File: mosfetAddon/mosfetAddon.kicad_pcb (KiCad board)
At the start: 2 copper layers, 89 x 61 mm, 70 parts, among them J1 coil, J10 Conn_01x18_Male, J2 coil, J3 coil, J4 coil, J5 coil, J6 coil, J7 coil, J8 coil, J9 pow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

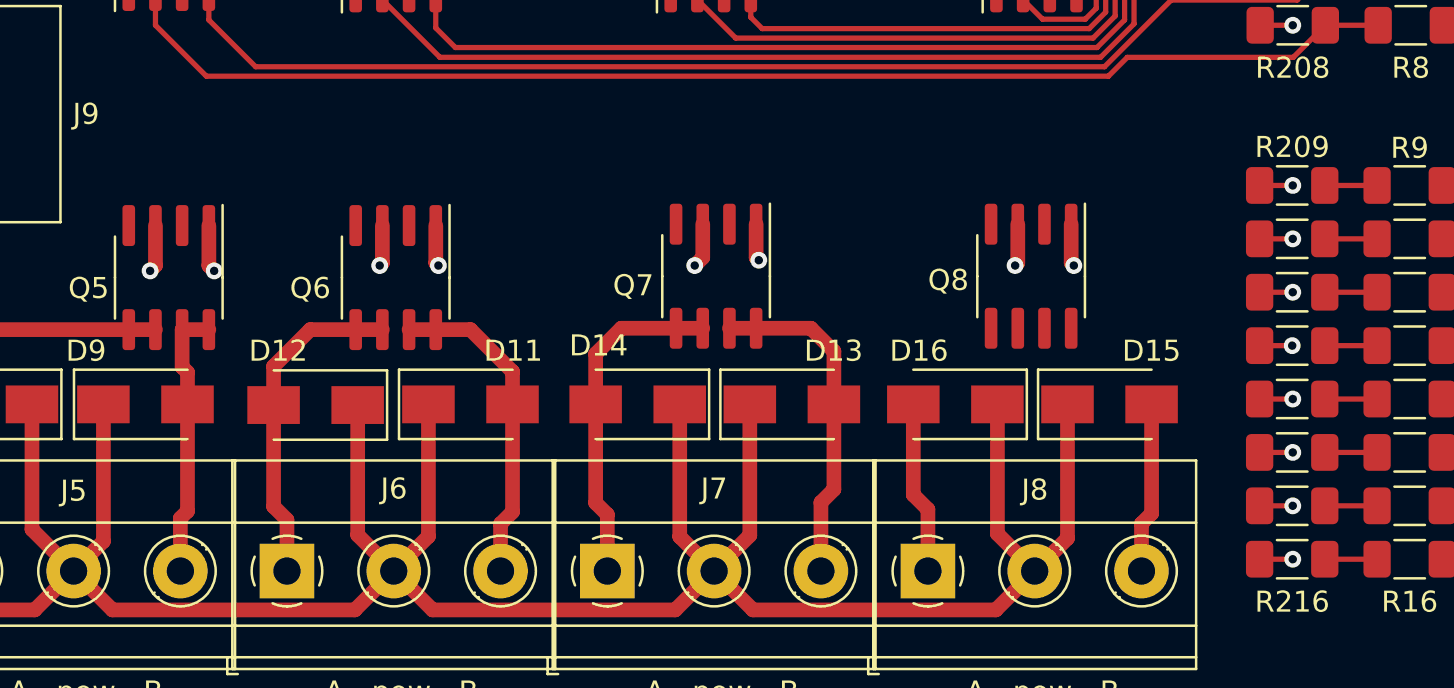
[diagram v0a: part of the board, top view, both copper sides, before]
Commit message: about to redo the PCB with an atmega 2560 instead. This will eliminate the need for 2 IO extenders and gives me the extra serial interface which I need. I also lack IO on the 328p
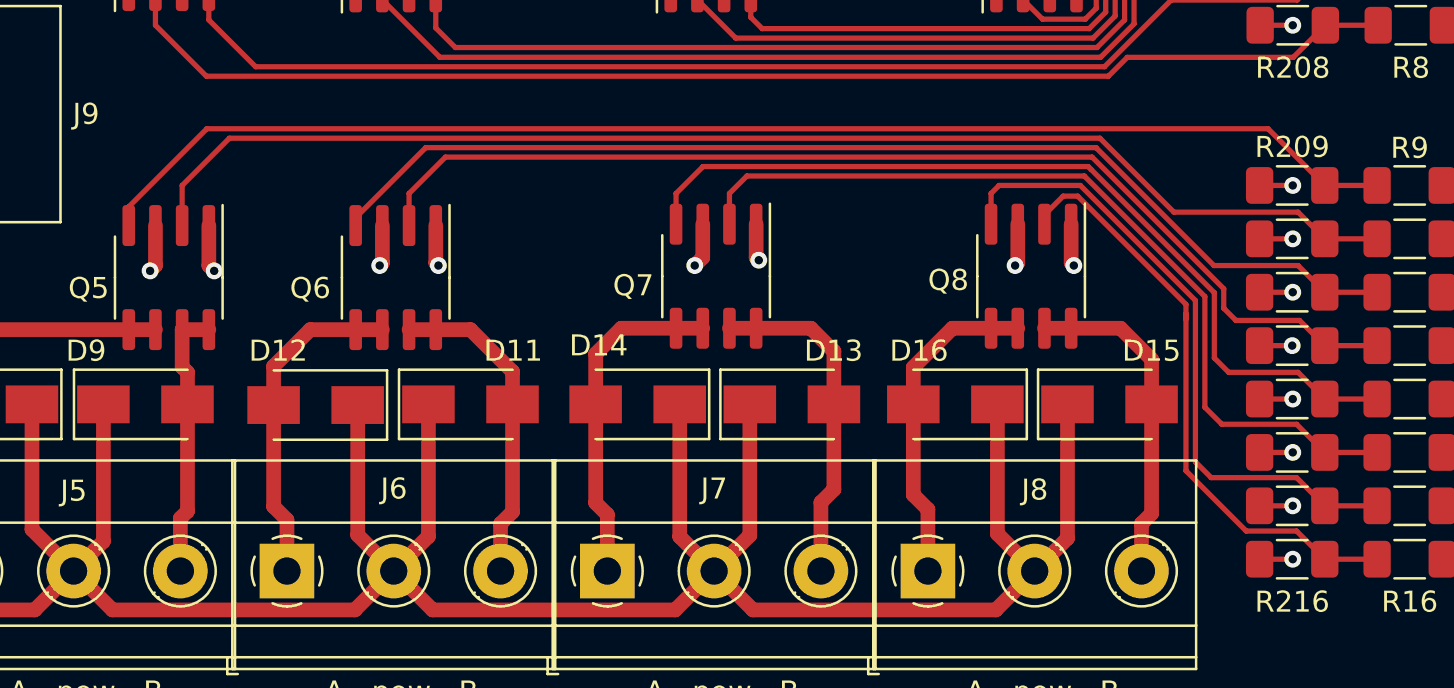
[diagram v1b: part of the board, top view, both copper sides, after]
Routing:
- net Net-(Q5-Pad4): track 2.49 -> 62.9 mm
- net Net-(Q5-Pad2): track 2.49 -> 61.7 mm
- net Net-(Q6-Pad4): track 2.49 -> 53.2 mm
- net Net-(Q6-Pad2): track 2.49 -> 52.6 mm
- net Net-(Q7-Pad4): track 2.49 -> 41.7 mm
- net Net-(Q7-Pad2): track 2.49 -> 41.1 mm
- net Net-(Q8-Pad4): track 2.49 -> 30.8 mm
- net Net-(Q8-Pad2): track 2.49 -> 28.7 mm
- net coil8L: track 8.13 -> 16.0 mm
- net coil8R: track 8.22 -> 15.7 mm
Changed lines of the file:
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@@
   (segment (start 146.22 135.298) (end 145.526 134.604) (width 0.7) (layer "F.Cu") (net 33))
   (segment (start 145.526 134.604) (end 145.526 130.302) (width 0.7) (layer "F.Cu") (net 33))
+  (segment (start 147.385 126.681) (end 145.526 128.54) (width 0.7) (layer "F.Cu") (net 33))
+  (segment (start 145.526 128.54) (end 145.526 130.302) (width 0.7) (layer "F.Cu") (net 33))
   (segment (start 146.22 138.231) (end 146.22 135.298) (width 0.7) (layer "F.Cu") (net 33))
+  (segment (start 150.495 126.681) (end 147.385 126.681) (width 0.7) (layer "F.Cu") (net 33))
+  (segment (start 151.765 126.681) (end 155.383 126.681) (width 0.7) (layer "F.Cu") (net 34))
+  (segment (start 156.86 128.158) (end 156.86 130.302) (width 0.7) (layer "F.Cu") (net 34))
   (segment (start 156.86 135.494) (end 156.86 130.302) (width 0.7) (layer "F.Cu") (net 34))
   (segment (start 156.38 138.231) (end 156.38 135.974) (width 0.7) (layer "F.Cu") (net 34))
   (segment (start 156.38 135.974) (end 156.86 135.494) (width 0.7) (layer "F.Cu") (net 34))
+  (segment (start 155.383 126.681) (end 156.86 128.158) (width 0.7) (layer "F.Cu") (net 34))
   (segment (start 153.70548 111.97852) (end 151.672448 111.97852) (width 0.25) (layer "F.Cu") (net 35))
   (segment (start 165.126 97.028) (end 167.614 97.028) (width 0.25) (layer "F.Cu") (net 35))
@@
   (segment (start 163.78552 111.06848) (end 157.794109 111.06848) (width 0.25) (layer "F.Cu") (net 42))
   (segment (start 114.24152 114.24152) (end 112.014 112.014) (width 0.25) (layer "F.Cu") (net 42))
+  (segment (start 162.40288 117.19088) (end 165.1 119.888) (width 0.25) (layer "F.Cu") (net 43))
+  (segment (start 111.91712 117.19088) (end 162.40288 117.19088) (width 0.25) (layer "F.Cu") (net 43))
+  (segment (start 108.204 121.796) (end 108.204 120.904) (width 0.25) (layer "F.Cu") (net 43))
+  (segment (start 108.204 120.904) (end 111.91712 117.19088) (width 0.25) (layer "F.Cu") (net 43))
   (segment (start 165.1 119.888) (end 167.588 119.888) (width 0.25) (layer "F.Cu") (net 43))
   (segment (start 167.588 122.428) (end 165.1 122.428) (width 0.25) (layer "F.Cu") (net 44))
+  (segment (start 112.9916 117.6404) (end 110.744 119.888) (width 0.25) (layer "F.Cu") (net 44))
+  (segment (start 154.40478 117.6404) (end 112.9916 117.6404) (width 0.25) (layer "F.Cu") (net 44))
+  (segment (start 110.744 119.888) (end 110.744 121.796) (width 0.25) (layer "F.Cu") (net 44))
+  (segment (start 163.83 121.158) (end 157.92238 121.158) (width 0.25) (layer "F.Cu") (net 44))
+  (segment (start 157.92238 121.158) (end 154.40478 117.6404) (width 0.25) (layer "F.Cu") (net 44))
+  (segment (start 165.1 122.428) (end 163.83 121.158) (width 0.25) (layer "F.Cu") (net 44))
   (segment (start 165.1 124.968) (end 167.588 124.968) (width 0.25) (layer "F.Cu") (net 45))
+  (segment (start 159.826662 123.698) (end 163.83 123.698) (width 0.25) (layer "F.Cu") (net 45))
+  (segment (start 163.83 123.698) (end 165.1 124.968) (width 0.25) (layer "F.Cu") (net 45))
+  (segment (start 122.329008 118.08992) (end 154.218582 118.08992) (width 0.25) (layer "F.Cu") (net 45))
+  (segment (start 154.218582 118.08992) (end 159.826662 123.698) (width 0.25) (layer "F.Cu") (net 45))
+  (segment (start 118.999 121.419928) (end 122.329008 118.08992) (width 0.25) (layer "F.Cu") (net 45))
+  (segment (start 118.999 121.796) (end 118.999 121.419928) (width 0.25) (layer "F.Cu") (net 45))
+  (segment (start 121.539 120.269) (end 121.539 121.796) (width 0.25) (layer "F.Cu") (net 46))
+  (segment (start 154.032384 118.53944) (end 123.26856 118.53944) (width 0.25) (layer "F.Cu") (net 46))
+  (segment (start 160.29408 125.73) (end 160.29408 124.801137) (width 0.25) (layer "F.Cu") (net 46))
+  (segment (start 123.26856 118.53944) (end 121.539 120.269) (width 0.25) (layer "F.Cu") (net 46))
+  (segment (start 160.87256 126.30848) (end 160.29408 125.73) (width 0.25) (layer "F.Cu") (net 46))
   (segment (start 167.588 127.508) (end 165.1 127.508) (width 0.25) (layer "F.Cu") (net 46))
+  (segment (start 163.90048 126.30848) (end 160.87256 126.30848) (width 0.25) (layer "F.Cu") (net 46))
+  (segment (start 165.1 127.508) (end 163.90048 126.30848) (width 0.25) (layer "F.Cu") (net 46))
+  (segment (start 160.29408 124.801137) (end 154.032384 118.53944) (width 0.25) (layer "F.Cu") (net 46))
+  (segment (start 135.51904 118.98896) (end 153.846184 118.98896) (width 0.25) (layer "F.Cu") (net 47))
+  (segment (start 163.83 128.778) (end 165.1 130.048) (width 0.25) (layer "F.Cu") (net 47))
+  (segment (start 134.239 120.269) (end 135.51904 118.98896) (width 0.25) (layer "F.Cu") (net 47))
+  (segment (start 160.528 128.778) (end 163.83 128.778) (width 0.25) (layer "F.Cu") (net 47))
+  (segment (start 159.84456 124.987335) (end 159.84456 128.09456) (width 0.25) (layer "F.Cu") (net 47))
+  (segment (start 153.846184 118.98896) (end 153.983225 119.126) (width 0.25) (layer "F.Cu") (net 47))
   (segment (start 165.1 130.048) (end 167.588 130.048) (width 0.25) (layer "F.Cu") (net 47))
+  (segment (start 153.983225 119.126) (end 159.84456 124.987335) (width 0.25) (layer "F.Cu") (net 47))
+  (segment (start 159.84456 128.09456) (end 160.528 128.778) (width 0.25) (layer "F.Cu") (net 47))
+  (segment (start 134.239 121.731) (end 134.239 120.269) (width 0.25) (layer "F.Cu") (net 47))
   (segment (start 167.588 132.588) (end 165.1 132.588) (width 0.25) (layer "F.Cu") (net 48))
+  (segment (start 137.60952 119.43848) (end 136.779 120.269) (width 0.25) (layer "F.Cu") (net 48))
+  (segment (start 165.1 132.588) (end 163.75952 131.24752) (width 0.25) (layer "F.Cu") (net 48))
+  (segment (start 163.75952 131.24752) (end 160.20352 131.24752) (width 0.25) (layer "F.Cu") (net 48))
+  (segment (start 136.779 120.269) (end 136.779 121.731) (width 0.25) (layer "F.Cu") (net 48))
+  (segment (start 153.659987 119.43848) (end 137.60952 119.43848) (width 0.25) (layer "F.Cu") (net 48))
+  (segment (start 159.39504 130.43904) (end 159.39504 125.173532) (width 0.25) (layer "F.Cu") (net 48))
+  (segment (start 160.20352 131.24752) (end 159.39504 130.43904) (width 0.25) (layer "F.Cu") (net 48))
+  (segment (start 159.39504 125.173532) (end 153.659987 119.43848) (width 0.25) (layer "F.Cu") (net 48))
+  (segment (start 153.47379 119.888) (end 149.606 119.888) (width 0.25) (layer "F.Cu") (net 49))
+  (segment (start 163.75952 133.78752) (end 159.69552 133.78752) (width 0.25) (layer "F.Cu") (net 49))
   (segment (start 165.1 135.128) (end 167.588 135.128) (width 0.25) (layer "F.Cu") (net 49))
+  (segment (start 159.69552 133.78752) (end 158.94552 133.03752) (width 0.25) (layer "F.Cu") (net 49))
+  (segment (start 158.94552 125.35973) (end 153.47379 119.888) (width 0.25) (layer "F.Cu") (net 49))
+  (segment (start 158.94552 133.03752) (end 158.94552 125.35973) (width 0.25) (layer "F.Cu") (net 49))
+  (segment (start 149.606 119.888) (end 149.225 120.269) (width 0.25) (layer "F.Cu") (net 49))
+  (segment (start 149.225 120.269) (end 149.225 121.731) (width 0.25) (layer "F.Cu") (net 49))
+  (segment (start 165.1 135.128) (end 163.75952 133.78752) (width 0.25) (layer "F.Cu") (net 49))
+  (segment (start 158.496 126.238) (end 158.496 125.984) (width 0.25) (layer "F.Cu") (net 50))
+  (segment (start 158.496 125.545928) (end 153.346072 120.396) (width 0.25) (layer "F.Cu") (net 50))
+  (segment (start 158.496 133.461493) (end 158.496 126.238) (width 0.25) (layer "F.Cu") (net 50))
+  (segment (start 153.346072 120.396) (end 152.654 120.396) (width 0.25) (layer "F.Cu") (net 50))
+  (segment (start 158.496 126.238) (end 158.496 125.545928) (width 0.25) (layer "F.Cu") (net 50))
   (segment (start 167.588 137.668) (end 165.1 137.668) (width 0.25) (layer "F.Cu") (net 50))
+  (segment (start 165.1 137.668) (end 163.75952 136.32752) (width 0.25) (layer "F.Cu") (net 50))
+  (segment (start 151.765 121.285) (end 152.654 120.396) (width 0.25) (layer "F.Cu") (net 50))
+  (segment (start 151.765 121.731) (end 151.765 121.285) (width 0.25) (layer "F.Cu") (net 50))
+  (segment (start 161.362027 136.32752) (end 158.496 133.461493) (width 0.25) (layer "F.Cu") (net 50))
+  (segment (start 163.75952 136.32752) (end 161.362027 136.32752) (width 0.25) (layer "F.Cu") (net 50))
   (zone (net 1) (net_name "GND") (layer "B.Cu") (hatch edge 0.508)
     (connect_pads (clearance 0.508))
